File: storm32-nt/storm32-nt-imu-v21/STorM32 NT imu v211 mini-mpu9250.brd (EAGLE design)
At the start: 13 x 18.4 mm, 13 parts, among them IC1 STM32F10XTXU6, Q1 RESONATORSMD

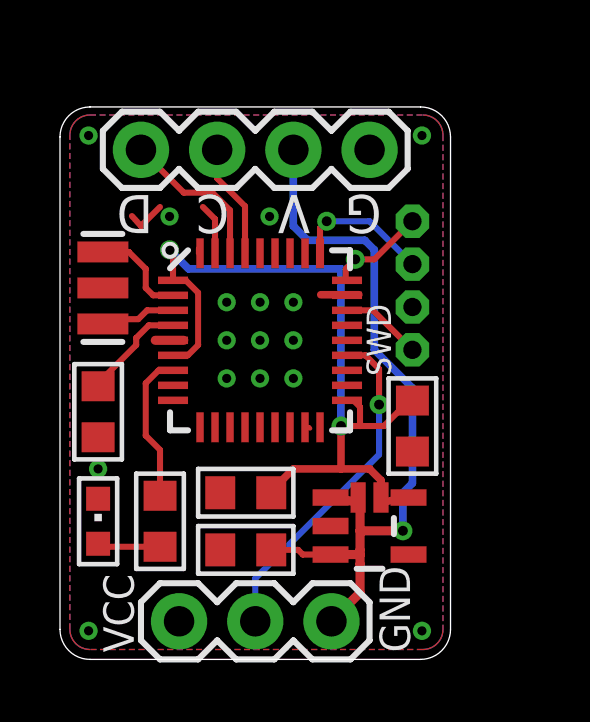
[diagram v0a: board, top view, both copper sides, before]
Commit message: release NT imu v2.11, NT encoder motor v2.51E, display v1.3
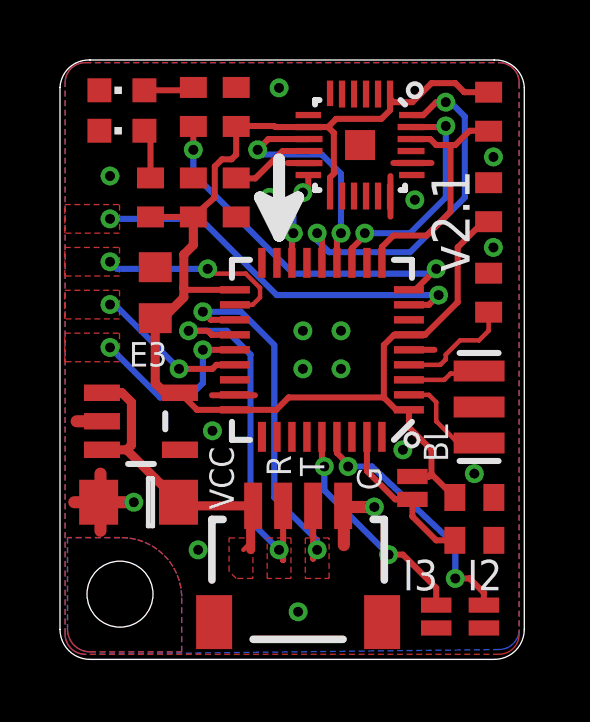
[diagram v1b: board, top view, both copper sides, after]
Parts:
- removed JP1: (no value), # SparkFun2:1X03
- removed JP2: SWD, # stdlib:4X1_1P27_OCT_BILEX
- removed JP3: (no value), # SparkFun2:1X04
- added C5, C6, C8: 100n, rcl:C0402
- added C7: 10n, rcl:C0402
- added IC3: MPU9250, # SparkFun2:QFN-24-3X3
- added LED2: green, led:CHIPLED_0603
- added NT: NT, con-jst2:SM04B-SRSS-TB
- added R2: 4.7k, rcl:R0402
- added R3: 2.2k, rcl:R0402
- added R5: 10k, rcl:R0402
- added SJ2: IMU-ID2, # SparkFun2:SJ_2S-NO
- added SJ3: IMU-ID3, # SparkFun2:SJ_2S-NO
- C1: value 100n -> 10u/10V; device rcl:C0603 -> rcl:C0805
- C3, C4: device rcl:C0603 -> rcl:C0402
- IC1: value STM32F10XTXU6 -> STM32F103T8
- IC2: value (none) -> TC1015-3.3VCT713
- LED1: value green -> red
- Q1: value RESONATORSMD -> CSTCE8M00G55-R0
- R1: value 2.2k -> 10k; device rcl:R0603 -> rcl:R0402
- SJ1: value POWER -> BOOT0
- moved C4 14.8 mm to (14.3, 15.2), turned to 90 degrees
- moved Q1 13.2 mm to (14.0, 8.41), turned to 90 degrees
- moved LED1 13.0 mm to (2.06, 17.6), turned to 90 degrees
- moved R1 10.5 mm to (13.8, 3.97), turned to 180 degrees
- moved IC2 8.38 mm to (2.70, 7.94)
- moved C2 7.32 mm to (3.17, 12.2), turned to 90 degrees
- moved C3 5.12 mm to (14.3, 12.2), turned to 90 degrees
- moved C1 3.91 mm to (2.62, 5.24)
- moved IC1 2.09 mm to (8.73, 10.3), turned to 180 degrees
- moved SJ1 1.46 mm to (11.7, 5.71), turned to 270 degrees
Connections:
- removed net SCL: IC1.33, JP3.2
- removed net SDA: IC1.34, JP3.1
- new net ADC1: IC1.8
- new net CANRX: IC1.23
- new net CANTX: IC1.24
- new net CS: IC1.10, IC3.22, R5.1
- new net INT: IC1.16, IC3.12
- new net N$20: C8.1, IC3.10
- new net N$3: IC1.35, R1.2, SJ1.2
- new net N$4: IC1.32, SJ3.2
- new net N$7: IC1.33, SJ2.2
- new net N$9: LED1.A, R2.2
- new net SCK: IC1.12, IC3.23
- new net SDI: IC1.14, IC3.24
- new net SDO: IC1.13, IC3.9
- new net T1CH1: IC1.20
- net 3.3V: now also C4.1, C5.1, C6.1, C7.1, IC3.1, IC3.13, IC3.8, R2.1, R5.2, SJ1.1; no longer C3.1, JP2.1, SJ1.2
- net 5V: now also NT.1; no longer JP1.1, JP3.3, SJ1.1
- net GND: now also C5.2, C6.2, C7.2, C8.2, IC1.30, IC1.31, IC3.11, IC3.18, IC3.20, LED2.C, NT.4, R1.1, SJ2.1, SJ3.1; no longer IC1.24, IC1.29, IC1.32, IC1.35, JP1.3, JP2.3, JP3.4
- net LED: now also IC1.9, R3.1; no longer IC1.7, R1.1
- net N$1: now also C3.1; no longer C4.1
- net N$2: now also LED2.A, R3.2; no longer LED1.A, R1.2
- net RX: now also NT.2; no longer JP1.2
- net SWCLK: no longer JP2.2
- net SWDIO: no longer JP2.4
- net TX: now also NT.3
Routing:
- net 3.3V: track 31.3 -> 47.1 mm, vias 3 -> 0
- net 5V: track 25.7 -> 11.5 mm, vias 1 -> 0
- net TX: track 0.00 -> 13.5 mm, vias 0 -> 2
- net ADC1: track 0.00 -> 13.1 mm, vias 0 -> 2
- net SDI: track 0.00 -> 12.0 mm, vias 0 -> 2
- net N$7: track 0.00 -> 8.43 mm, vias 0 -> 2
- net CS: track 0.00 -> 8.40 mm
- net SDO: track 0.00 -> 8.00 mm, vias 0 -> 2
- net SCK: track 0.00 -> 7.91 mm, vias 0 -> 2
- net N$4: track 0.00 -> 7.47 mm, vias 0 -> 2
- net GND: track 5.80 -> 13.2 mm, vias 16 -> 17
- net LED: track 5.04 -> 12.3 mm, vias 0 -> 2
- net T1CH1: track 0.00 -> 6.62 mm, vias 0 -> 2
- net CANRX: track 0.00 -> 6.16 mm, vias 0 -> 2
- net N$3: track 0.00 -> 5.37 mm
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- added copper zone on layer 1, net 5V
- added copper zone on layer 1, net ADC1
- added copper zone on layer 1, net CANRX
- added copper zone on layer 1, net CANTX
- added copper zone on layer 1, net RX
- added copper zone on layer 1, net T1CH1
- added copper zone on layer 1, net TX
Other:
- board size 13 x 18.4 mm -> 15.5 x 20 mm
- board text added: "ADC1 EXT0"
- board text added: "BL"
- board text added: "CANRX EXT3"
- board text added: "CANTX EXT2"
- board text added: "E3"
- board text added: "I2"
- board text added: "I3"
- board text added: "NT IMU mpu9250"
- board text added: "R"
- board text added: "RX"
- board text added: "T"
- board text added: "T1CH1 EXT1"
- board text added: "TX"
- board text added: "v2.1"
- board text added: "www.olliw.eu"
- board text removed: "C"
- board text removed: "D"
- board text removed: "Rx"
- board text removed: "SWD"
- board text removed: "V"
- board text removed: "www.olliw.eu OLed v1.2"
